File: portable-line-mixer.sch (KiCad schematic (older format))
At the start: 17 parts, among them J1 JACK-TRS, U1 RC4560, U2 RC4560

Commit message: Reworking with new power supply and layout
also changing to kicad 5 style library layout and management
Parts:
- removed C1, C2: 27pF, Capacitors_SMD:C_0805_HandSoldering, symbol C
- removed C3, C4: 47pF, Capacitors_SMD:C_0805_HandSoldering, symbol C
- removed C5, C6: 10uF, Capacitors_Tantalum_SMD:TantalC_SizeR_EIA-2012, symbol CP_Small
- removed J1: JACK-TRS, SW-CUI-INC:SJ1-353XNG-3Pin, symbol JACK-TRS
- removed R1, R2, R3, R4: 10k, Resistors_SMD:R_0805_HandSoldering, symbol R
- removed R34, R35: 4k7, Capacitors_SMD:C_0805_HandSoldering, symbol R
- removed R5, R6: 100R, Resistors_SMD:R_0805_HandSoldering, symbol R
- removed U1, U2: RC4560, Housings_SSOP:TSSOP-8_4.4x3mm_Pitch0.65mm, symbol RC4560
- added MK1, MK2, MK3, MK4: Mounting_Hole_PAD, MountingHole:MountingHole_4.3mm_M4_Pad_Via, symbol Mechanical:Mounting_Hole_PAD
- added MK5, MK6, MK7, MK8: Mounting_Hole_PAD, MountingHole:MountingHole_2.7mm_M2.5_Pad_Via, symbol Mechanical:Mounting_Hole_PAD
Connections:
- net labels removed: +12VA, +5VD, -12VA, SCL, SDA, ~CE
- wire segments 119 -> 29
- no-connect marks 1 -> 0
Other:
- note added: "All signal directions are indicated from the\nperspective of the MUX box\n\n8x connectors with stereo audio out, mono mic in, \nPTT in, Mic Mute in, +5V bias out\nEach connector can be used for one or more functions.\nThese connectors are for speakermics, headsets and ptt switches.\nConnector model is Amphenol LTW circular connector 8 pin\n\n8x connectors with stereo audio in, mono mic out, PTT o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"
- note added: "Board Mounting Holes"
- note removed: "Each input module has jack, pot and summing resistor = 10k\n\n+5VA = analog +5V, +5VD = digital +5V, (separate regulators)\n-5V, GNDREF = global ground"
- note removed: "LEFT"
- note removed: "Potential connection\nfor an LCD display"
- note removed: "RIGHT"

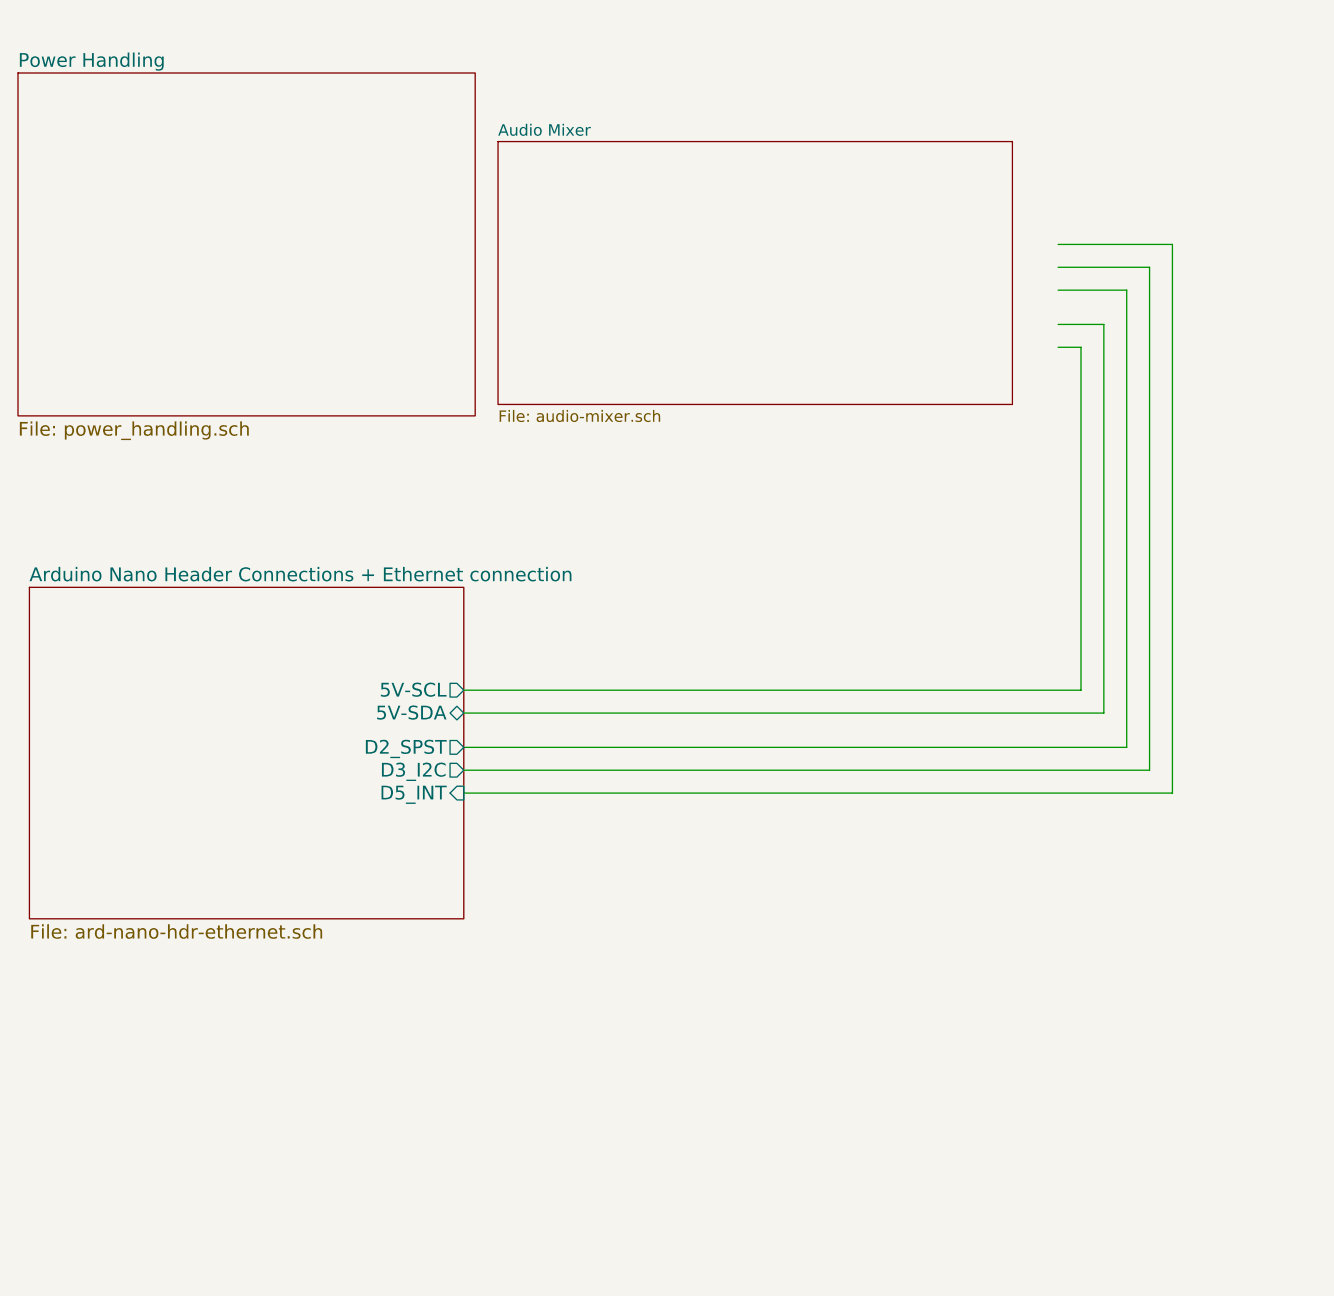
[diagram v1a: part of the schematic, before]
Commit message: Updated Schematics
- added ethernet
- swapped to using prebuilt nano
- swapped to using db25 connector
- swapped other connectors
- added connectors for an LCD screen
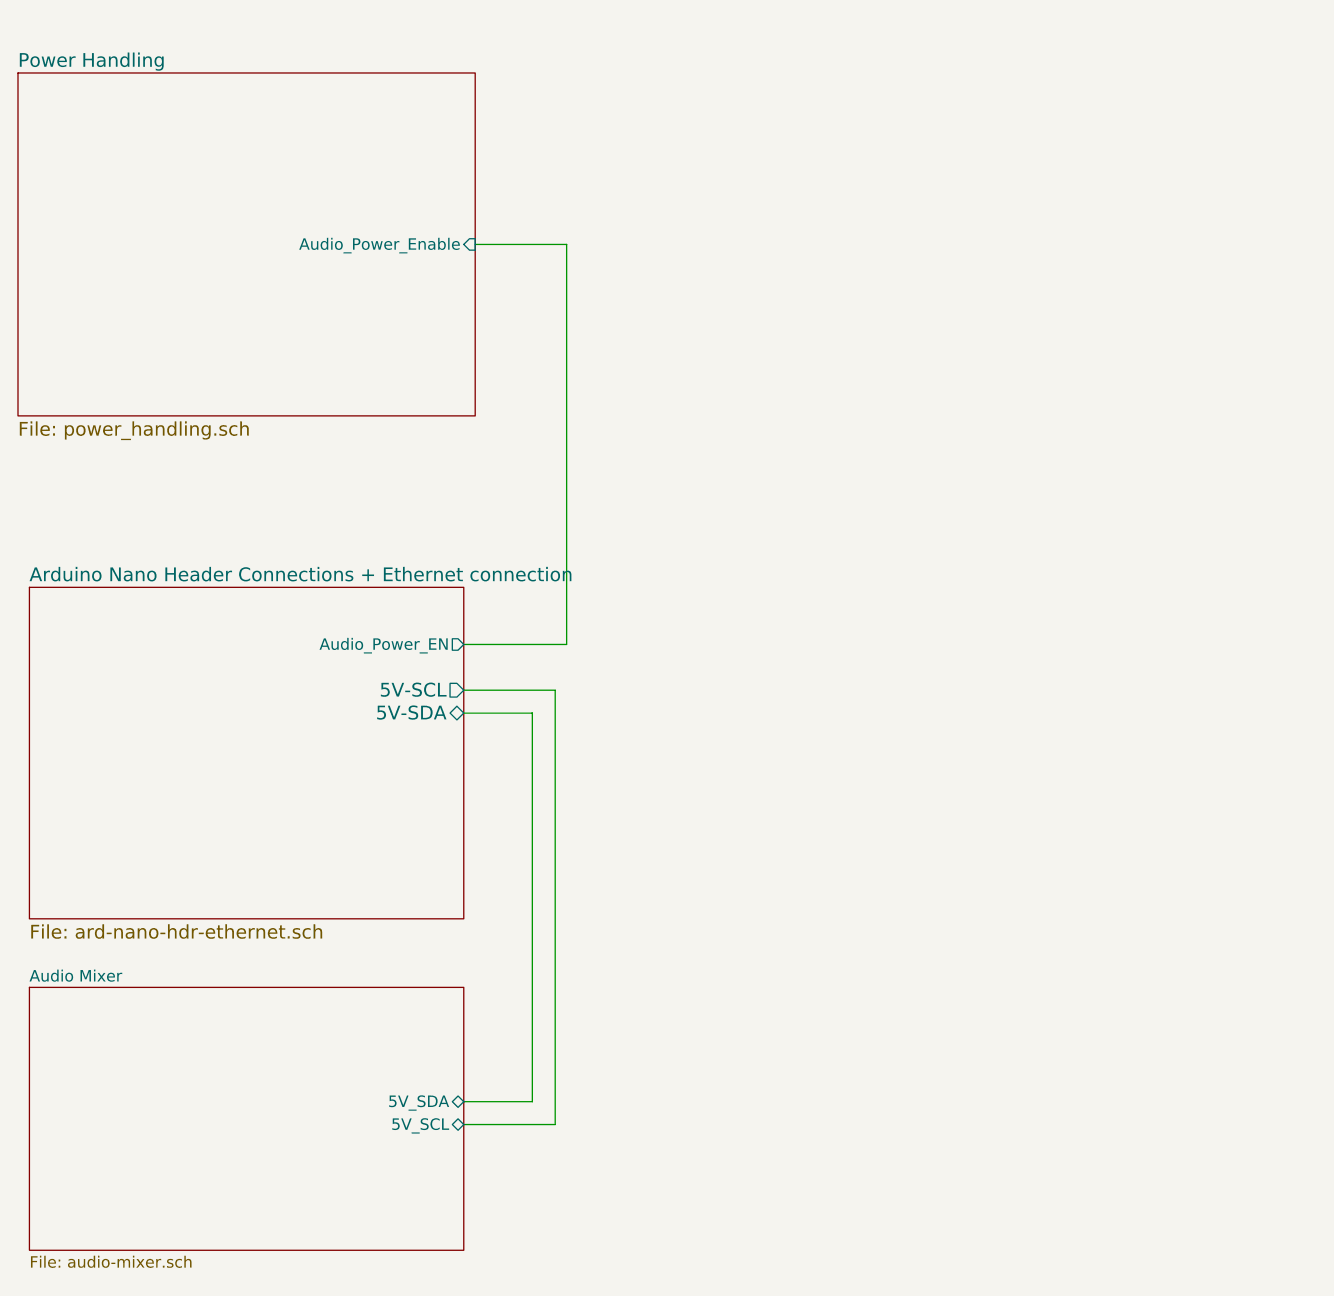
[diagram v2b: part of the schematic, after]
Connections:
- wire segments 29 -> 23
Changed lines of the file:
@@
 F0 "Power Handling" 60
 F1 "power_handling.sch" 60
+F2 "Audio_Power_Enable" I R 2900 1600 50
 $EndSheet
 $Sheet
@@
 F2 "5V-SDA" B R 2850 3650 60
 F3 "5V-SCL" O R 2850 3550 60
-F4 "D2_SPST" O R 2850 3800 60
-F5 "D3_I2C" O R 2850 3900 60
-F6 "D5_INT" I R 2850 4000 60
+F4 "Audio_Power_EN" O R 2850 3350 50
 $EndSheet
 Text Notes 6950 6200 0    60   ~ 0
 All signal directions are indicated from the\nperspective of the MUX box\n\n8x connectors with stereo audio out, mono mic in, \nPTT in, Mic Mute in, +5V bias out\nEach connector can be used for one or more functions.\nThese connectors are for speakermics, headsets and ptt switches.\nConnector model is Amphenol LTW circular connector 8 pin\n\n8x connectors with stereo audio in, mono mic out, PTT out\nEach connector can be used for one or more functions.\nThese connectors are for smartphones and radios.\nConnector model is Amphenol LTW circular connector 8pin\n\n1x DB25 connector to connect to mixer\n1x TRS connector for output from mixer to MUX\n\n
-Wire Wire Line
-	5450 2050 5550 2050
-Wire Wire Line
-	5550 2050 5550 3550
-Wire Wire Line
-	5550 3550 2850 3550
-Wire Wire Line
-	5450 1950 5650 1950
-Wire Wire Line
-	5650 1950 5650 3650
-Wire Wire Line
-	5650 3650 2850 3650
-Wire Wire Line
-	5450 1800 5750 1800
-Wire Wire Line
-	5750 1800 5750 3800
-Wire Wire Line
-	5750 3800 2850 3800
-Wire Wire Line
-	5450 1700 5850 1700
-Wire Wire Line
-	5850 1700 5850 3900
-Wire Wire Line
-	5850 3900 2850 3900
-Wire Wire Line
-	5450 1600 5950 1600
-Wire Wire Line
-	5950 1600 5950 4000
-Wire Wire Line
-	5950 4000 2850 4000
 $Comp
 L Mechanical:Mounting_Hole_PAD MK1
@@
 	6900 800  6900 3050
 $Sheet
-S 3000 1150 2250 1150
+S 950  4850 1900 1150
 U 5AC2500F
 F0 "Audio Mixer" 50
 F1 "audio-mixer.sch" 50
+F2 "5V_SDA" B R 2850 5350 50
+F3 "5V_SCL" B R 2850 5450 50
 $EndSheet
+Wire Wire Line
+	2850 5350 3150 5350
+Wire Wire Line
+	3150 5350 3150 3650
+Wire Wire Line
+	3150 3650 2850 3650
+Wire Wire Line
+	2850 3550 3250 3550
+Wire Wire Line
+	3250 3550 3250 5450
+Wire Wire Line
+	3250 5450 2850 5450
+Wire Wire Line
+	2850 3350 3300 3350
+Wire Wire Line
+	3300 3350 3300 1600
+Wire Wire Line
+	3300 1600 2900 1600
 $EndSCHEMATC

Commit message: Portable Line Mixer done
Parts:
- removed MK4: Mounting_Hole_PAD, MountingHole:MountingHole_4.3mm_M4_Pad_Via, symbol Mechanical:Mounting_Hole_PAD
- MK1, MK2, MK3: footprint MountingHole:MountingHole_4.3mm_M4_Pad_Via -> MountingHole:MountingHole_2.7mm_M2.5_Pad_Via
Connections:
- wire segments 23 -> 22
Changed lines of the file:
@@
 F 0 "MK1" H 7400 1251 50  0000 L CNN
 F 1 "Mounting_Hole_PAD" H 7400 1160 50  0000 L CNN
-F 2 "MountingHole:MountingHole_4.3mm_M4_Pad_Via" H 7300 1200 50  0001 C CNN
+F 2 "MountingHole:MountingHole_2.7mm_M2.5_Pad_Via" H 7300 1200 50  0001 C CNN
 F 3 "" H 7300 1200 50  0001 C CNN
 	1    7300 1200
@@
 F 0 "MK2" H 8300 1251 50  0000 L CNN
 F 1 "Mounting_Hole_PAD" H 8300 1160 50  0000 L CNN
-F 2 "MountingHole:MountingHole_4.3mm_M4_Pad_Via" H 8200 1200 50  0001 C CNN
+F 2 "MountingHole:MountingHole_2.7mm_M2.5_Pad_Via" H 8200 1200 50  0001 C CNN
 F 3 "" H 8200 1200 50  0001 C CNN
 	1    8200 1200
 	1    0    0    -1
-$EndComp
-$Comp
-L Mechanical:Mounting_Hole_PAD MK4
-U 1 1 5AA439B1
-P 8200 1600
-F 0 "MK4" H 8100 1558 50  0000 R CNN
-F 1 "Mounting_Hole_PAD" H 8100 1649 50  0000 R CNN
-F 2 "MountingHole:MountingHole_4.3mm_M4_Pad_Via" H 8200 1600 50  0001 C CNN
-F 3 "" H 8200 1600 50  0001 C CNN
-	1    8200 1600
-	-1   0    0    1
 $EndComp
 $Comp
@@
 F 0 "MK3" H 7200 1558 50  0000 R CNN
 F 1 "Mounting_Hole_PAD" H 7200 1649 50  0000 R CNN
-F 2 "MountingHole:MountingHole_4.3mm_M4_Pad_Via" H 7300 1600 50  0001 C CNN
+F 2 "MountingHole:MountingHole_2.7mm_M2.5_Pad_Via" H 7300 1600 50  0001 C CNN
 F 3 "" H 7300 1600 50  0001 C CNN
 	1    7300 1600
@@
 	7300 1500 7300 1400
 Wire Wire Line
-	8200 1500 8200 1400
-Wire Wire Line
 	8200 1400 7300 1400
-Connection ~ 8200 1400
 Wire Wire Line
 	8200 1400 8200 1300
